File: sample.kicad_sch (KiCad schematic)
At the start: 4 parts, among them J1 Conn_02x08_Odd_Even, J2 Conn_02x15_Odd_Even, J3 Conn_02x10_Odd_Even, J4 Conn_02x17_Odd_Even

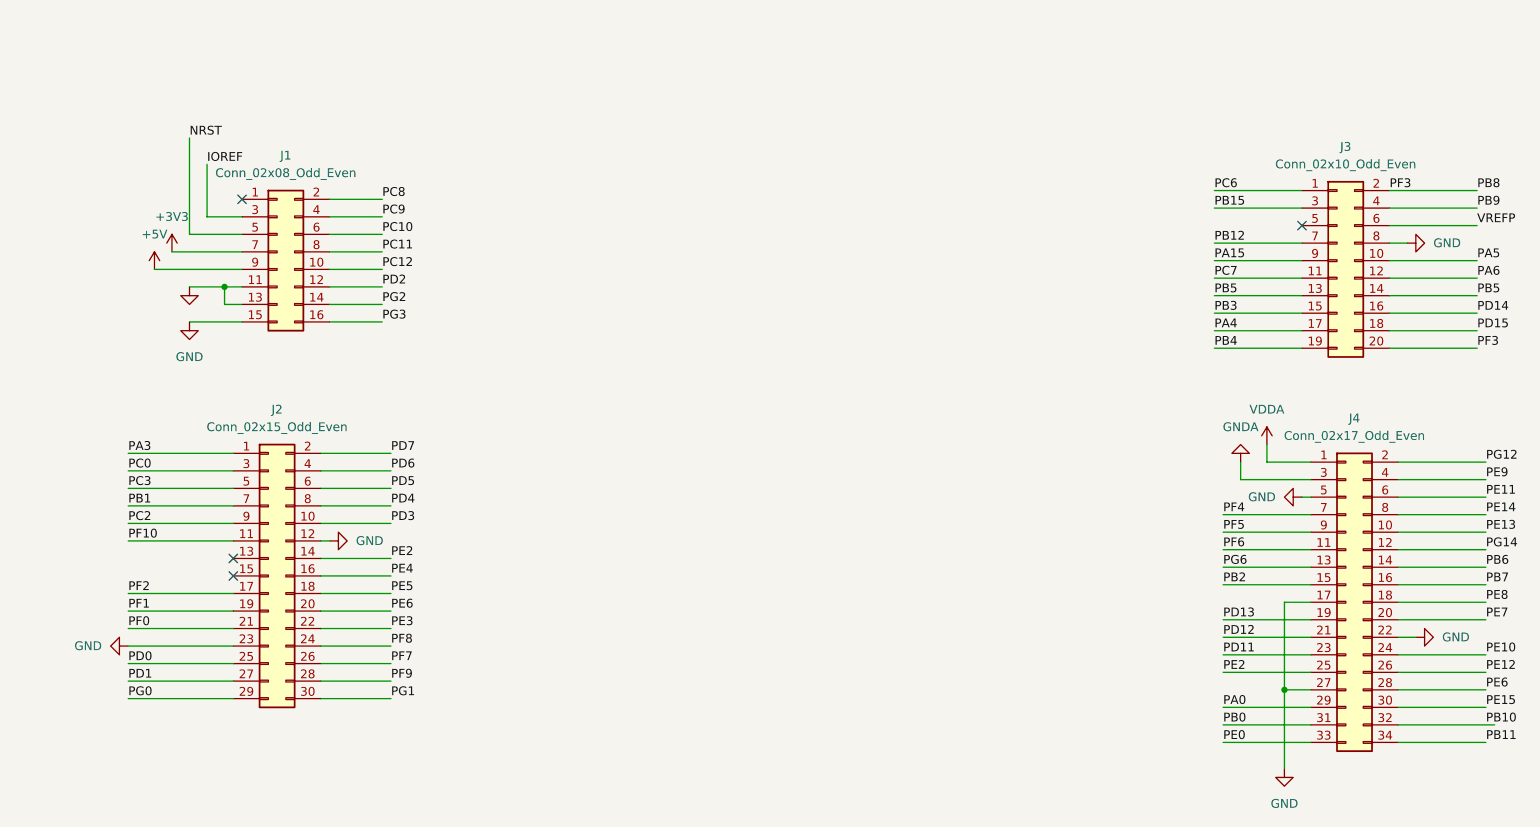
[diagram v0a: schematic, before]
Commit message: split into hirachical pages
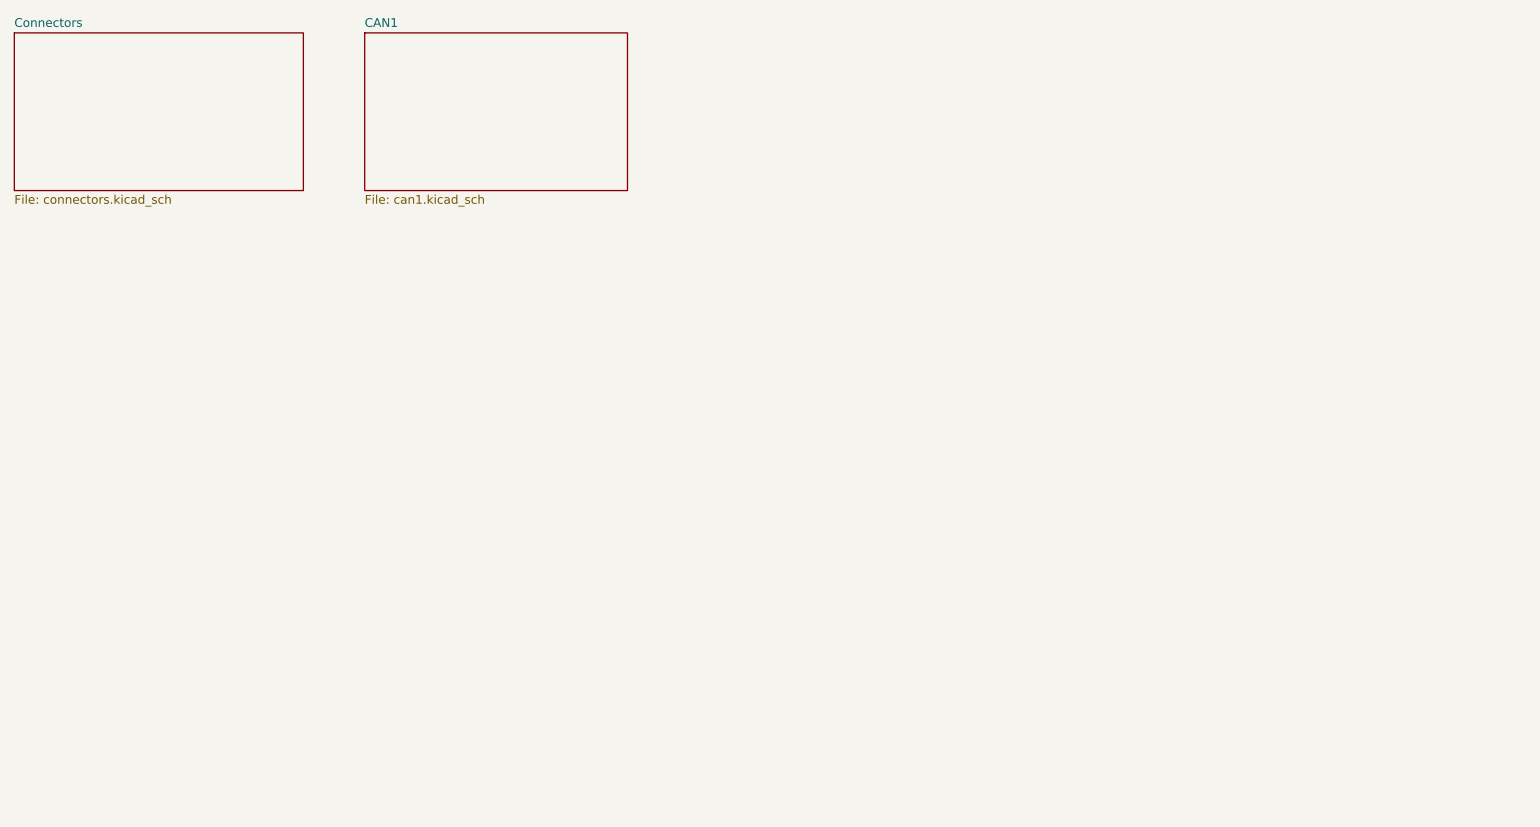
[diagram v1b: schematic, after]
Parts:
- removed J1: Conn_02x08_Odd_Even, Connector_PinHeader_2.54mm:PinHeader_2x08_P2.54mm_Vertical, symbol Connector_Generic:Conn_02x08_Odd_Even
- removed J2: Conn_02x15_Odd_Even, Connector_PinHeader_2.54mm:PinHeader_2x15_P2.54mm_Vertical, symbol Connector_Generic:Conn_02x15_Odd_Even
- removed J3: Conn_02x10_Odd_Even, Connector_PinHeader_2.54mm:PinHeader_2x10_P2.54mm_Vertical, symbol Connector_Generic:Conn_02x10_Odd_Even
- removed J4: Conn_02x17_Odd_Even, Connector_PinHeader_2.54mm:PinHeader_2x17_P2.54mm_Vertical, symbol Connector_Generic:Conn_02x17_Odd_Even
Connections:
- no-connect marks 4 -> 0
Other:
- added sheet CAN1 (can1.kicad_sch)
- added sheet Connectors (connectors.kicad_sch)

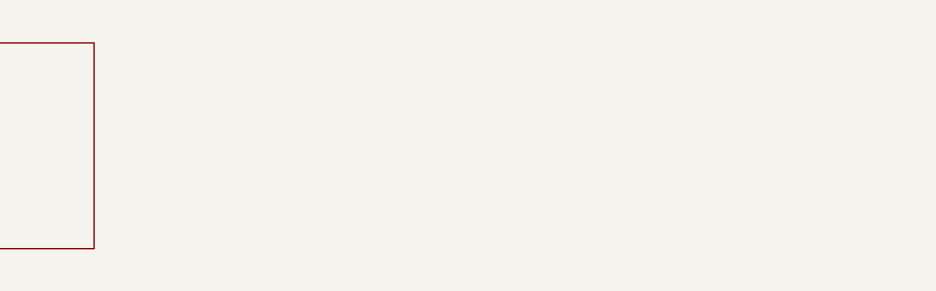
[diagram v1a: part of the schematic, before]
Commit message: add CAN2 and CAN3
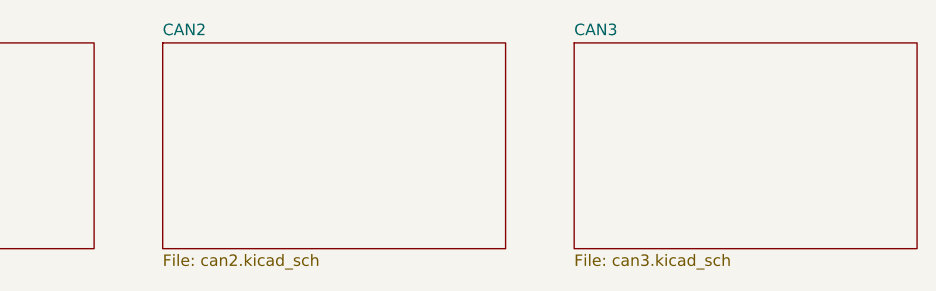
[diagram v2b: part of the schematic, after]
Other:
- added sheet CAN2 (can2.kicad_sch)
- added sheet CAN3 (can3.kicad_sch)
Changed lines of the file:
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@@
+		)
+	)
+	(sheet
+		(at 113.03 15.24)
+		(size 38.1 22.86)
+		(fields_autoplaced yes)
+		(stroke
+			(width 0.1524)
+			(type solid)
+		)
+		(fill
+			(color 0 0 0 0.0000)
+		)
+		(property "Sheetname" "CAN2"
+			(at 113.03 14.5284 0)
+			(effects
+				(font
+					(size 1.27 1.27)
+				)
+				(justify left bottom)
+			)
+		)
+		(property "Sheetfile" "can2.kicad_sch"
+			(at 113.03 38.6846 0)
+			(effects
+				(font
+					(size 1.27 1.27)
+				)
+				(justify left top)
+			)
+		)
+		(instances
+			(project "sample"
+				(path "/b24c09df-2e49-4fc3-a45d-ba0b1ff2d257"
+					(page "4")
+				)
+			)
+		)
+	)
+	(sheet
+		(at 158.75 15.24)
+		(size 38.1 22.86)
+		(fields_autoplaced yes)
+		(stroke
+			(width 0.1524)
+			(type solid)
+		)
+		(fill
+			(color 0 0 0 0.0000)
+		)
+		(property "Sheetname" "CAN3"
+			(at 158.75 14.5284 0)
+			(effects
+				(font
+					(size 1.27 1.27)
+				)
+				(justify left bottom)
+			)
+		)
+		(property "Sheetfile" "can3.kicad_sch"
+			(at 158.75 38.6846 0)
+			(effects
+				(font
+					(size 1.27 1.27)
+				)
+				(justify left top)
+			)
+		)
+		(instances
+			(project "sample"
+				(path "/b24c09df-2e49-4fc3-a45d-ba0b1ff2d257"
+					(page "5")
+				)
+			)
 		)
 	)

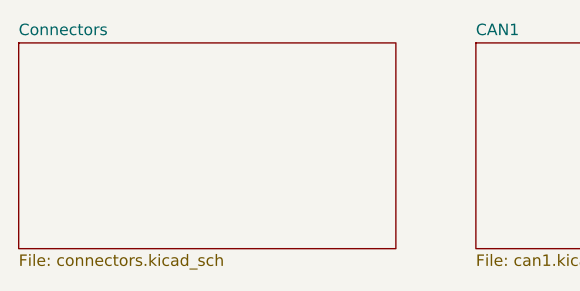
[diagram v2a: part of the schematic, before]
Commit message: move connectors to zio_connectors
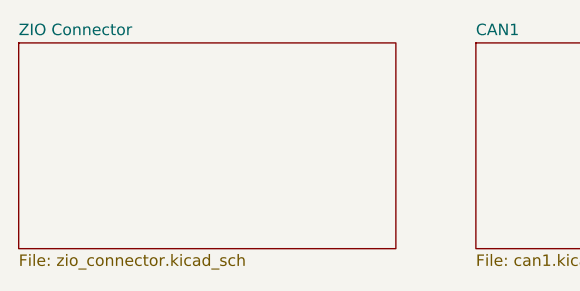
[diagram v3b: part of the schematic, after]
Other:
- sheet Connectors renamed ZIO Connector
- sheet ZIO Connector: file connectors.kicad_sch -> zio_connector.kicad_sch
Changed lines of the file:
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@@
 			(color 0 0 0 0.0000)
 		)
-		(property "Sheetname" "Connectors"
+		(property "Sheetname" "ZIO Connector"
 			(at 16.51 14.5284 0)
 			(effects
@@
 			)
 		)
-		(property "Sheetfile" "connectors.kicad_sch"
+		(property "Sheetfile" "zio_connector.kicad_sch"
 			(at 16.51 38.6846 0)
 			(effects

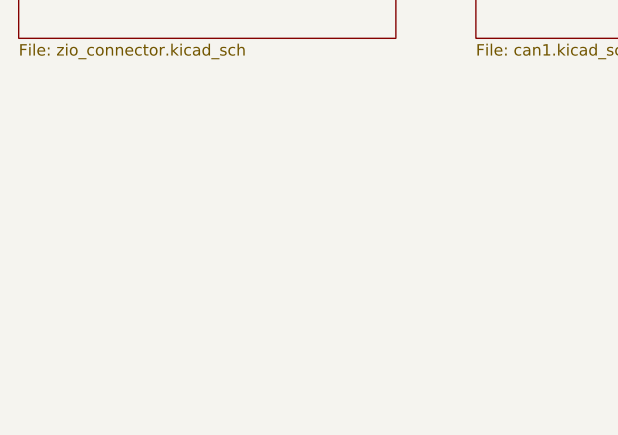
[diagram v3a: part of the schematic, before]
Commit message: add CAN Sub-D connectors
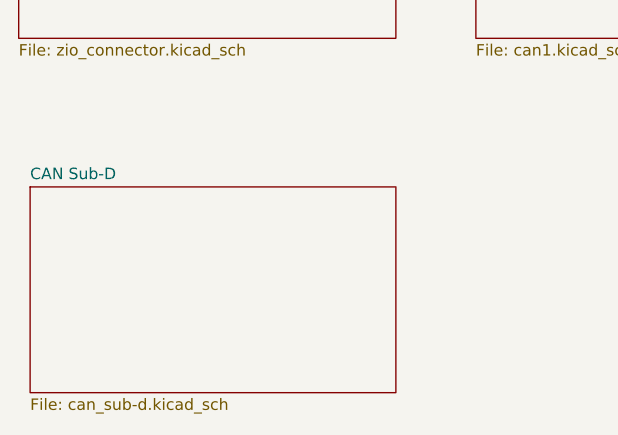
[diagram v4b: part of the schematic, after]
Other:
- added sheet CAN Sub-D (can_sub-d.kicad_sch)
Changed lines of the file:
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@@
 	(paper "A4")
+	(sheet
+		(at 17.78 54.61)
+		(size 40.64 22.86)
+		(fields_autoplaced yes)
+		(stroke
+			(width 0.1524)
+			(type solid)
+		)
+		(fill
+			(color 0 0 0 0.0000)
+		)
+		(property "Sheetname" "CAN Sub-D"
+			(at 17.78 53.8984 0)
+			(effects
+				(font
+					(size 1.27 1.27)
+				)
+				(justify left bottom)
+			)
+		)
+		(property "Sheetfile" "can_sub-d.kicad_sch"
+			(at 17.78 78.0546 0)
+			(effects
+				(font
+					(size 1.27 1.27)
+				)
+				(justify left top)
+			)
+		)
+		(instances
+			(project "sample"
+				(path "/b24c09df-2e49-4fc3-a45d-ba0b1ff2d257"
+					(page "6")
+				)
+			)
+		)
+	)
 	(sheet
 		(at 67.31 15.24)

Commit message: route uarts
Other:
- added sheet UARTs (uarts.kicad_sch)
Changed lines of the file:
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@@
+	)
+	(sheet
+		(at 68.58 54.61)
+		(size 38.1 22.86)
+		(fields_autoplaced yes)
+		(stroke
+			(width 0.1524)
+			(type solid)
+		)
+		(fill
+			(color 0 0 0 0.0000)
+		)
+		(property "Sheetname" "UARTs"
+			(at 68.58 53.8984 0)
+			(effects
+				(font
+					(size 1.27 1.27)
+				)
+				(justify left bottom)
+			)
+		)
+		(property "Sheetfile" "uarts.kicad_sch"
+			(at 68.58 78.0546 0)
+			(effects
+				(font
+					(size 1.27 1.27)
+				)
+				(justify left top)
+			)
+		)
+		(instances
+			(project "sample"
+				(path "/b24c09df-2e49-4fc3-a45d-ba0b1ff2d257"
+					(page "7")
+				)
+			)
+		)
 	)
 	(sheet
